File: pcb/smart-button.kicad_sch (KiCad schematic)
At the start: 5 parts, among them J2 Conn_01x15, SW1 SW_Push, SW2 SW_Push, SW3 SW_Push

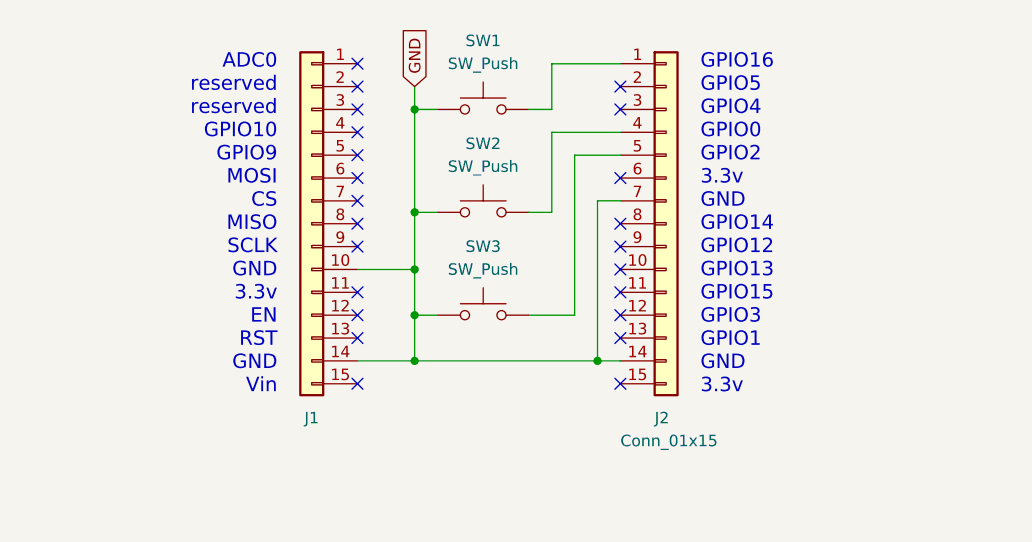
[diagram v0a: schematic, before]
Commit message: Added resistors seperatly
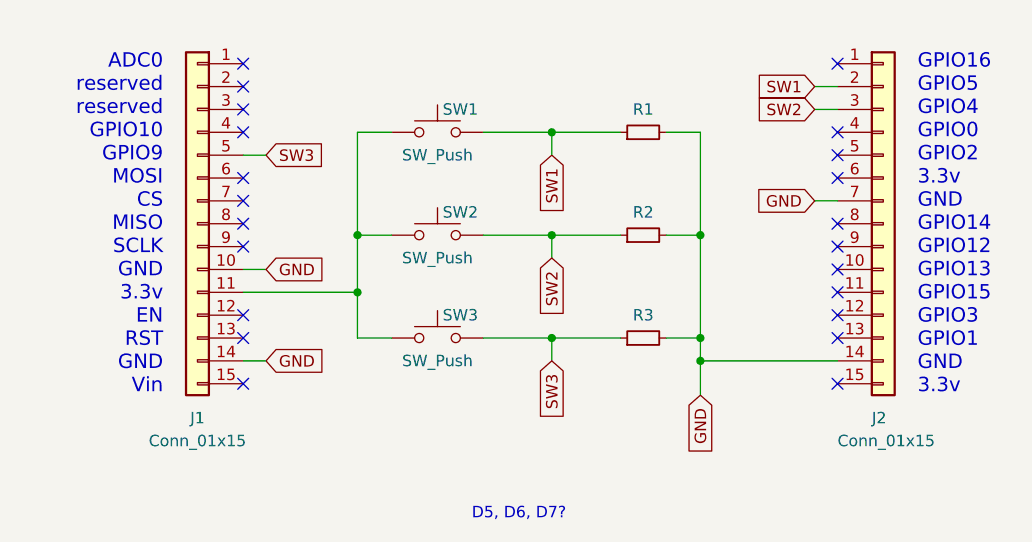
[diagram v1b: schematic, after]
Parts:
- added R1, R2, R3: (no value), symbol Device:R_Small
- J1: value (none) -> Conn_01x15; footprint (none) -> Connector_PinHeader_2.54mm:PinHeader_1x15_P2.54mm_Vertical
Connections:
- net GND: now also R1.2, R2.2, R3.2; no longer SW1.1, SW2.1, SW3.1
- net at J2.1 (Pin_1): no longer SW1.2
- net at J1.11 (Pin_11): now also SW1.1, SW2.1, SW3.1
- net SW3: now reaches J1.5 (Pin_5)
- net SW3: now also SW3.2, R3.1
- net at J2.5 (Pin_5): no longer SW3.2
- net SW1: now reaches J2.2 (Pin_2)
- net SW1: now also SW1.2, R1.1
- net SW2: now reaches J2.3 (Pin_3)
- net SW2: now also SW2.2, R2.1
- net at J2.4 (Pin_4): no longer SW2.2
- no-connect marks 23 -> 22
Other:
- note added: "D5, D6, D7?"
- moved on the sheet: J1, J2, SW1, SW2, SW3

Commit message: Using simple pins not connected to leds and verified internal pull-up resistors
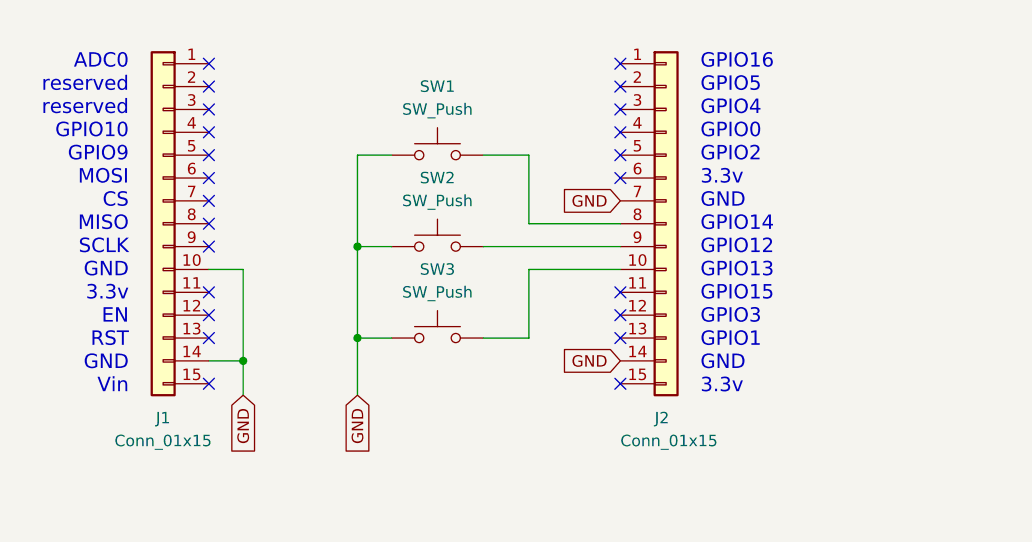
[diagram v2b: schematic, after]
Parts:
- removed R1, R2, R3: (no value), symbol Device:R_Small
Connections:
- net GND: now also SW1.1, SW2.1, SW3.1
- net at J2.10 (Pin_10): now also SW3.2
- net at J2.8 (Pin_8): now also SW1.2
- net at J2.9 (Pin_9): now also SW2.2
- net SW1: no longer names the net of J2.2 (Pin_2)
- net SW1: no longer SW1.2
- net SW2: no longer names the net of J2.3 (Pin_3)
- net SW2: no longer SW2.2
- net SW3: no longer names the net of J1.5 (Pin_5)
- net SW3: no longer SW3.2
- now unconnected: J1.11 (Pin_11)
- no-connect marks 22 -> 23
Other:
- note removed: "D5, D6, D7?"
- moved on the sheet: J1, J2, SW1, SW2
